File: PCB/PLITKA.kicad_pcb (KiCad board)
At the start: 2 copper layers, 120.5 x 85.5 mm, 47 parts, among them SW1 SW_SPDT_321, SW10 MX_SW_HS, SW11 MX_SW_HS, SW12 MX_SW_HS, SW13 MX_SW_HS, SW14 MX_SW_HS, SW15 MX_SW_HS, SW16 MX_SW_HS, SW17 MX_SW_HS, SW18 MX_SW_HS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

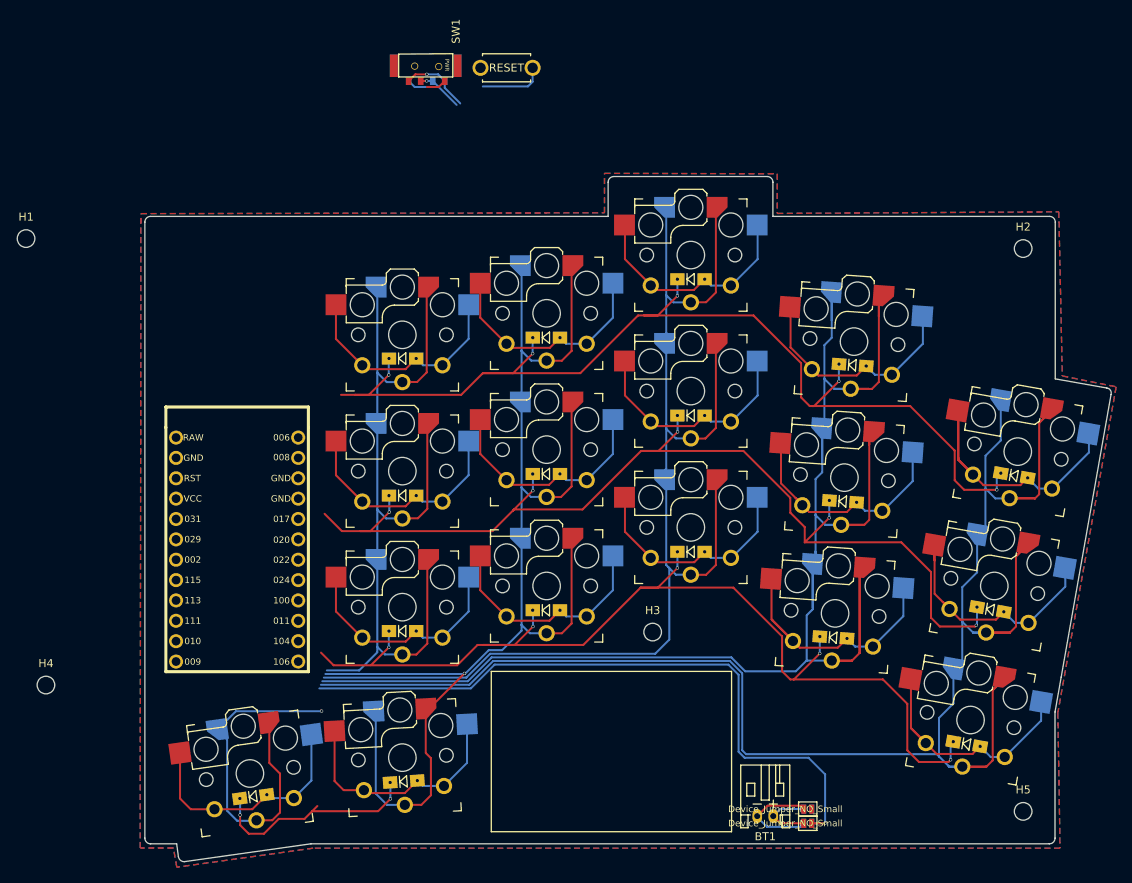
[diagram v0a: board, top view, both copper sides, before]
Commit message: Pulled updates of the footprints
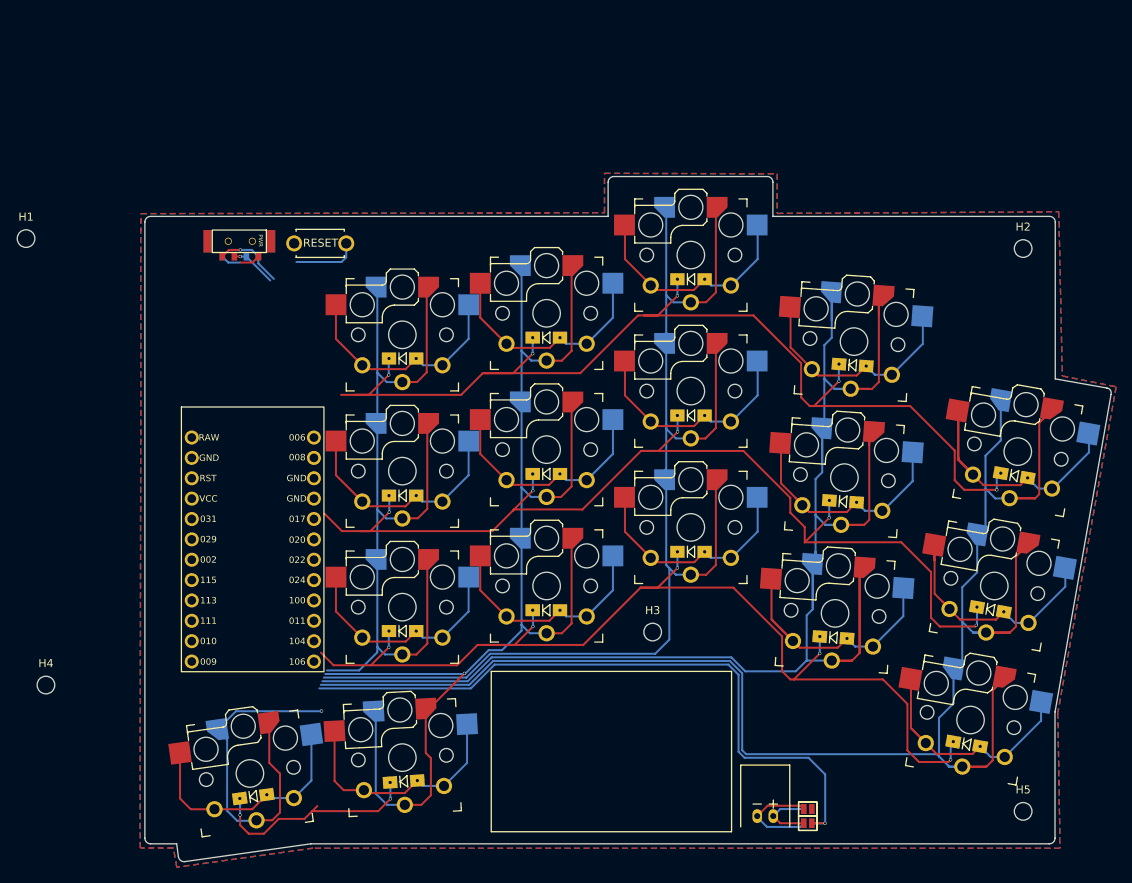
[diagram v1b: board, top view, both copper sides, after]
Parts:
- moved SW19 31.9 mm to (106.7, 56.9)
- moved SW1 31.9 mm to (100.5, 55.4)
